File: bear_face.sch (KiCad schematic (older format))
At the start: 190 parts, among them J1 USB_B_Micro, SW1 SW_Push, U1 ATmega32U4-AU, Y1 16MHz

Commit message: Footprints updated
Changed footprints to copies saved in 'bear_face_parts' for ease of cloning
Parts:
- D1, D10, D11, D12, D13, D14, D15, D16, D17, D18, D19, D2, D20, D21, D22, D23, D24, D25, D26, D27, D28, D29, D3, D30, D31, D32, D33, D34, D35, D36, D37, D38, D39, D4, D40, D41, D42, D43, D44, D45, D46, D47, D48, D49, D5, D50, D51, D52, D53, D54, D55, D56, D57, D58, D59, D6, D60, D61, D62, D63, D64, D65, D66, D67, D68, D69, D7, D70, D71, D72, D73, D74, D75, D76, D77, D78, D79, D8, D80, D81, D82, D83, D9: footprint Keebio-Parts:Diode -> bear_face_parts:Diode-THT
- MX1, MX15, MX31, MX44: footprint MX_Only:MXOnly-1.5U-NoLED -> bear_face_parts:MXOnly-1.5U-NoLED
- MX10, MX11, MX12, MX13, MX14, MX16, MX17, MX18, MX19, MX2, MX20, MX21, MX22, MX23, MX24, MX25, MX26, MX27, MX28, MX3, MX30, MX32, MX33, MX34, MX35, MX36, MX37, MX38, MX39, MX4, MX40, MX41, MX42, MX43, MX45, MX47, MX48, MX49, MX5, MX50, MX51, MX52, MX53, MX54, MX55, MX56, MX57, MX59, MX6, MX61, MX62, MX63, MX64, MX65, MX66, MX67, MX68, MX69, MX7, MX70, MX72, MX73, MX78, MX79, MX8, MX80, MX81, MX82, MX83, MX9: footprint MX_Only:MXOnly-1U-NoLED -> bear_face_parts:MXOnly-1U-NoLED
- MX29: footprint MX_Only:MXOnly-2U-NoLED -> bear_face_parts:MXOnly-2U-NoLED
- MX46, MX71: footprint MX_Only:MXOnly-1.75U-NoLED -> bear_face_parts:MXOnly-1.75U-NoLED
- MX58, MX60: footprint MX_Only:MXOnly-2.25U-NoLED -> bear_face_parts:MXOnly-2.25U-NoLED
- MX74, MX75, MX76: footprint MX_Only:MXOnly-1.25U-NoLED -> bear_face_parts:MXOnly-1.25U-NoLED
- MX77: footprint MX_Only:MXOnly-6.25U-ReversedStabilizers-NoLED -> bear_face_parts:MXOnly-6.25U-ReversedStabilizers-NoLED
- SW1: footprint random-keyboard-parts:PushButton_6x6mm_TH_Pretty -> bear_face_parts:PushButton_6x6mm_TH_Pretty

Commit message: Initial SMD commit
Diodes changed to SMD, short tracks added to pad2 and between adjacent diodes
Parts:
- D1, D10, D11, D12, D13, D14, D15, D16, D17, D18, D19, D2, D20, D21, D22, D23, D24, D25, D26, D27, D28, D29, D3, D30, D31, D32, D33, D34, D35, D36, D37, D38, D39, D4, D40, D41, D42, D43, D44, D45, D46, D47, D48, D49, D5, D50, D51, D52, D53, D54, D55, D56, D57, D58, D59, D6, D60, D61, D62, D63, D64, D65, D66, D67, D68, D69, D7, D70, D71, D72, D73, D74, D75, D76, D77, D78, D79, D8, D80, D81, D82, D83, D9: footprint bear_face_parts:Diode-THT -> bear_face_parts:D_SOD-123

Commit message: Changed RESET switch to SMD
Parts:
- SW1: footprint bear_face_parts:PushButton_6x6mm_TH_Pretty -> random-keyboard-parts:SKQG-1155865
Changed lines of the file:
@@
 F 0 "SW1" H 1400 4085 50  0000 C CNN
 F 1 "SW_Push" H 1400 3994 50  0000 C CNN
-F 2 "bear_face_parts:PushButton_6x6mm_TH_Pretty" H 1400 4000 50  0001 C CNN
+F 2 "random-keyboard-parts:SKQG-1155865" H 1400 4000 50  0001 C CNN
 F 3 "~" H 1400 4000 50  0001 C CNN
 	1    1400 3800

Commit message: dPairs, left side MCU tracked
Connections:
- net RD-: now reaches R3.1, U1.3 (D-)
- net RD+: now reaches R2.1, U1.4 (D+)
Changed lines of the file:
@@
 L power:+5V #PWR0110
 U 1 1 5E4994F7
-P 1350 4600
-F 0 "#PWR0110" H 1350 4450 50  0001 C CNN
-F 1 "+5V" H 1365 4773 50  0000 C CNN
-F 2 "" H 1350 4600 50  0001 C CNN
-F 3 "" H 1350 4600 50  0001 C CNN
-	1    1350 4600
+P 1700 4600
+F 0 "#PWR0110" H 1700 4450 50  0001 C CNN
+F 1 "+5V" H 1715 4773 50  0000 C CNN
+F 2 "" H 1700 4600 50  0001 C CNN
+F 3 "" H 1700 4600 50  0001 C CNN
+	1    1700 4600
 	1    0    0    -1
 $EndComp
@@
 Wire Wire Line
 	750  4450 1100 4450
-Wire Wire Line
-	1350 4600 1800 4600
-Wire Wire Line
-	1300 4800 1800 4800
-Wire Wire Line
-	1000 4900 1800 4900
 $Comp
 L Connector:USB_B_Micro J1
@@
 Text GLabel 3000 6700 2    50   Input ~ 0
 ROW5
-Text GLabel 3000 6400 2    50   Input ~ 0
-COL0
-Text GLabel 3000 6600 2    50   Input ~ 0
-COL1
-Text GLabel 3000 6500 2    50   Input ~ 0
-COL2
 Text GLabel 3000 6200 2    50   Input ~ 0
 COL3
@@
 NoConn ~ 3000 4700
 NoConn ~ 3000 4800
+Text GLabel 1350 4800 1    50   Input ~ 0
+RD+
+Text GLabel 1050 4900 3    50   Input ~ 0
+RD-
+Wire Wire Line
+	1700 4600 1800 4600
+Connection ~ 1050 4900
+Connection ~ 1350 4800
+Wire Wire Line
+	1050 4900 1800 4900
+Wire Wire Line
+	1000 4900 1050 4900
+Wire Wire Line
+	1350 4800 1800 4800
+Wire Wire Line
+	1300 4800 1350 4800
+Text GLabel 3000 6500 2    50   Input ~ 0
+COL2
+Text GLabel 3000 6600 2    50   Input ~ 0
+COL1
+Text GLabel 3000 6400 2    50   Input ~ 0
+COL0
 $EndSCHEMATC

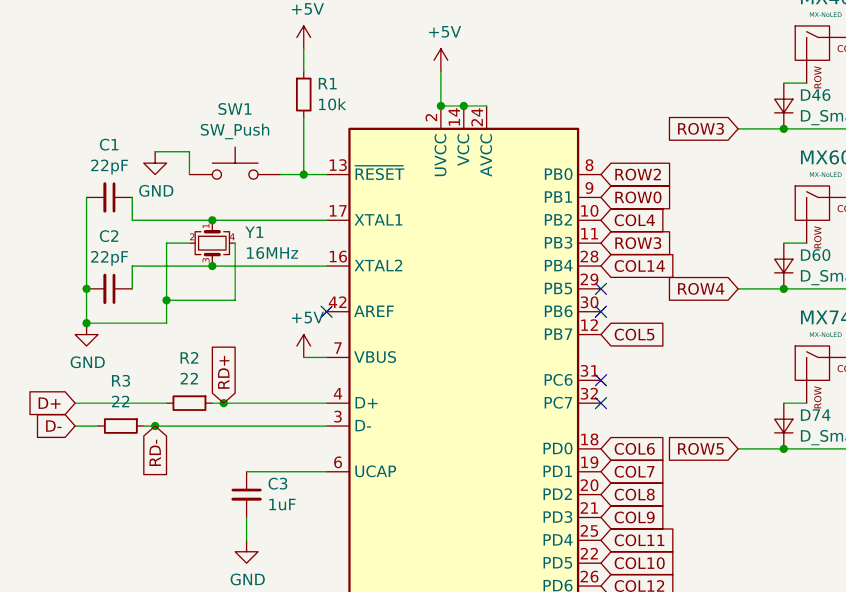
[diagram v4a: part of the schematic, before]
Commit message: Tracks finished, DRC check passed, tracks and vias cleaned up
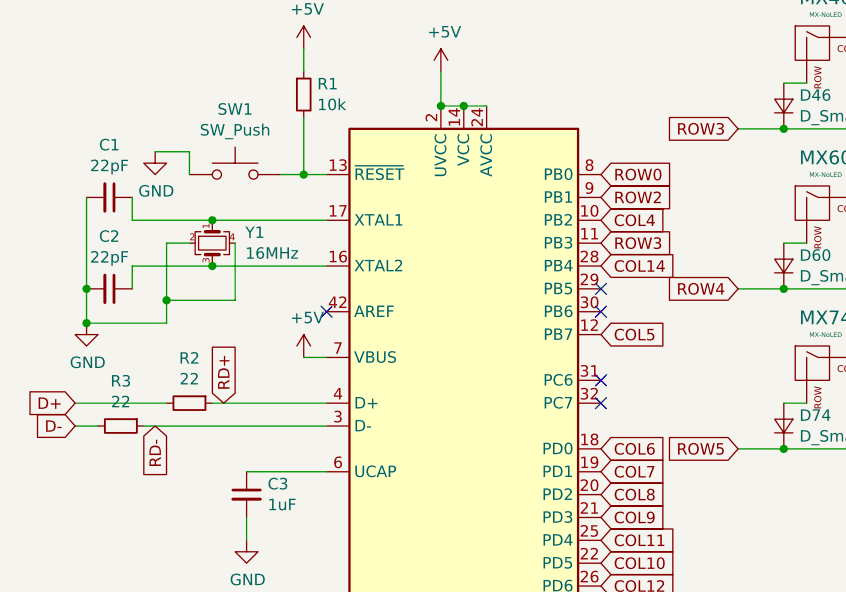
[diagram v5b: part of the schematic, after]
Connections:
- net ROW0: now also U1.8 (PB0); no longer U1.9 (PB1)
- net ROW2: now also U1.9 (PB1); no longer U1.8 (PB0)
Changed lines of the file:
@@
 COL3
 NoConn ~ 1800 4400
-Text GLabel 3000 3900 2    50   Input ~ 0
+Text GLabel 3000 3800 2    50   Input ~ 0
 ROW0
 Text GLabel 3000 6000 2    50   Input ~ 0
 ROW1
-Text GLabel 3000 3800 2    50   Input ~ 0
+Text GLabel 3000 3900 2    50   Input ~ 0
 ROW2
 Text GLabel 3000 4100 2    50   Input ~ 0
@@
 Text GLabel 3000 6300 2    50   Input ~ 0
 ROW4
-NoConn ~ 3000 4300
-NoConn ~ 3000 4400
-NoConn ~ 3000 4700
-NoConn ~ 3000 4800
 Text GLabel 1350 4800 1    50   Input ~ 0
 RD+
@@
 Wire Wire Line
 	1700 4600 1800 4600
-Connection ~ 1050 4900
-Connection ~ 1350 4800
-Wire Wire Line
-	1050 4900 1800 4900
-Wire Wire Line
-	1000 4900 1050 4900
-Wire Wire Line
-	1350 4800 1800 4800
-Wire Wire Line
-	1300 4800 1350 4800
 Text GLabel 3000 6500 2    50   Input ~ 0
 COL2
@@
 Text GLabel 3000 6400 2    50   Input ~ 0
 COL0
+Wire Wire Line
+	1000 4900 1800 4900
+Wire Wire Line
+	1300 4800 1800 4800
+NoConn ~ 3000 4300
+NoConn ~ 3000 4400
+NoConn ~ 3000 4700
+NoConn ~ 3000 4800
 $EndSCHEMATC

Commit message: Load caps moved closer, minor MCU track tweaks, USB-Micro changed to molex
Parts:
- J1: footprint Connector_USB:USB_Micro-B_Wuerth_629105150521 -> Connector_USB:USB_Micro-B_GCT_USB3076-30-A
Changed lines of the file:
@@
 F 0 "J1" H 1257 2867 50  0000 C CNN
 F 1 "USB_B_Micro" H 1257 2776 50  0000 C CNN
-F 2 "Connector_USB:USB_Micro-B_Wuerth_629105150521" H 1350 2350 50  0001 C CNN
+F 2 "Connector_USB:USB_Micro-B_GCT_USB3076-30-A" H 1350 2350 50  0001 C CNN
 F 3 "~" H 1350 2350 50  0001 C CNN
 	1    1200 2400

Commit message: Initial branch commit
Footprint SilkS updated to be on desired sides, all components placed
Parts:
- added Q1: 2N7002, Package_TO_SOT_SMD:SOT-23, symbol Transistor_FET:2N7002
- added R1, R10, R11, R12, R13, R14, R15, R16, R17, R18, R19, R2, R20, R21, R22, R23, R24, R25, R26, R27, R28, R29, R3, R30, R31, R32, R33, R34, R35, R36, R37, R38, R39, R4, R40, R41, R42, R43, R44, R45, R46, R47, R48, R49, R5, R50, R51, R52, R53, R54, R55, R56, R57, R58, R59, R6, R60, R61, R62, R63, R64, R65, R66, R67, R68, R69, R7, R70, R71, R72, R73, R74, R75, R76, R77, R78, R79, R8, R80, R81, R82, R83, R9: 470, bear_face_parts:Resistor-THT, symbol Device:R_Small
- added R88: 4.7k, Keebio-Parts:Resistor, symbol Device:R_Small
- D1, D10, D11, D12, D13, D14, D15, D16, D17, D18, D19, D2, D20, D21, D22, D23, D24, D25, D26, D27, D28, D29, D3, D30, D31, D32, D33, D34, D35, D36, D37, D38, D39, D4, D40, D41, D42, D43, D44, D45, D46, D47, D48, D49, D5, D50, D51, D52, D53, D54, D55, D56, D57, D58, D59, D6, D60, D61, D62, D63, D64, D65, D66, D67, D68, D69, D7, D70, D71, D72, D73, D74, D75, D76, D77, D78, D79, D8, D80, D81, D82, D83, D9: footprint bear_face_parts:D_SOD-123 -> bear_face_parts:Diode-THT
- H1, H2, H3, H4, H5, H6, H7: footprint MountingHole:MountingHole_6mm -> bear_face_parts:MountingHole_6mm
- H8: footprint MountingHole:MountingHole_3mm -> bear_face_parts:MountingHole_3mm
- J1: footprint Connector_USB:USB_Micro-B_GCT_USB3076-30-A -> Connector_USB:USB_Micro-B_Wuerth_629105150521
- MX1, MX15, MX31, MX44: value MX-NoLED -> MX-LED; footprint bear_face_parts:MXOnly-1.5U-NoLED -> bear_face_parts:MXOnly-1.5U; symbol MX_Alps_Hybrid:MX-NoLED -> MX_Alps_Hybrid:MX-LED
- MX10, MX11, MX12, MX13, MX14, MX16, MX17, MX18, MX19, MX2, MX20, MX21, MX22, MX23, MX24, MX25, MX26, MX27, MX28, MX3, MX30, MX32, MX33, MX34, MX35, MX36, MX37, MX38, MX39, MX4, MX40, MX41, MX42, MX43, MX45, MX47, MX48, MX49, MX5, MX50, MX51, MX52, MX53, MX54, MX55, MX56, MX57, MX59, MX6, MX61, MX62, MX63, MX64, MX65, MX66, MX67, MX68, MX69, MX7, MX70, MX72, MX73, MX78, MX79, MX8, MX80, MX81, MX82, MX83, MX9: value MX-NoLED -> MX-LED; footprint bear_face_parts:MXOnly-1U-NoLED -> bear_face_parts:MXOnly-1U; symbol MX_Alps_Hybrid:MX-NoLED -> MX_Alps_Hybrid:MX-LED
- MX29: value MX-NoLED -> MX-LED; footprint bear_face_parts:MXOnly-2U-NoLED -> bear_face_parts:MXOnly-2U-NoStabs; symbol MX_Alps_Hybrid:MX-NoLED -> MX_Alps_Hybrid:MX-LED
- MX46, MX71: value MX-NoLED -> MX-LED; footprint bear_face_parts:MXOnly-1.75U-NoLED -> bear_face_parts:MXOnly-1.75U; symbol MX_Alps_Hybrid:MX-NoLED -> MX_Alps_Hybrid:MX-LED
- MX58, MX60: value MX-NoLED -> MX-LED; footprint bear_face_parts:MXOnly-2.25U-NoLED -> bear_face_parts:MXOnly-2.25U-NoStabs; symbol MX_Alps_Hybrid:MX-NoLED -> MX_Alps_Hybrid:MX-LED
- MX74, MX75, MX76: value MX-NoLED -> MX-LED; footprint bear_face_parts:MXOnly-1.25U-NoLED -> bear_face_parts:MXOnly-1.25U; symbol MX_Alps_Hybrid:MX-NoLED -> MX_Alps_Hybrid:MX-LED
- MX77: value MX-NoLED -> MX-LED; footprint bear_face_parts:MXOnly-6.25U-ReversedStabilizers-NoLED -> bear_face_parts:MXOnly-6.25U-NoStabs; symbol MX_Alps_Hybrid:MX-NoLED -> MX_Alps_Hybrid:MX-LED
- SW1: footprint random-keyboard-parts:SKQG-1155865 -> bear_face_parts:PushButton_6x6mm_TH_Pretty
- renumbered R1 to R84, R2 to R85, R3 to R86, R4 to R87
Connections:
- net +5V: now also MX1.3 (LED), MX10.3 (LED), MX11.3 (LED), MX12.3 (LED), MX13.3 (LED), MX14.3 (LED), MX15.3 (LED), MX16.3 (LED), MX17.3 (LED), MX18.3 (LED), MX19.3 (LED), MX2.3 (LED), MX20.3 (LED), MX21.3 (LED), MX22.3 (LED), MX23.3 (LED), MX24.3 (LED), MX25.3 (LED), MX26.3 (LED), MX27.3 (LED), MX28.3 (LED), MX29.3 (LED), MX3.3 (LED), MX30.3 (LED), MX31.3 (LED), MX32.3 (LED), MX33.3 (LED), MX34.3 (LED), MX35.3 (LED), MX36.3 (LED), MX37.3 (LED), MX38.3 (LED), MX39.3 (LED), MX4.3 (LED), MX40.3 (LED), MX41.3 (LED), MX42.3 (LED), MX43.3 (LED), MX44.3 (LED), MX45.3 (LED), MX46.3 (LED), MX47.3 (LED), MX48.3 (LED), MX49.3 (LED), MX5.3 (LED), MX50.3 (LED), MX51.3 (LED), MX52.3 (LED), MX53.3 (LED), MX54.3 (LED), MX55.3 (LED), MX56.3 (LED), MX57.3 (LED), MX58.3 (LED), MX59.3 (LED), MX6.3 (LED), MX60.3 (LED), MX61.3 (LED), MX62.3 (LED), MX63.3 (LED), MX64.3 (LED), MX65.3 (LED), MX66.3 (LED), MX67.3 (LED), MX68.3 (LED), MX69.3 (LED), MX7.3 (LED), MX70.3 (LED), MX71.3 (LED), MX72.3 (LED), MX73.3 (LED), MX74.3 (LED), MX75.3 (LED), MX76.3 (LED), MX77.3 (LED), MX78.3 (LED), MX79.3 (LED), MX8.3 (LED), MX80.3 (LED), MX81.3 (LED), MX82.3 (LED), MX83.3 (LED), MX9.3 (LED)
- net GND: now also Q1.2 (S), R88.2
- net LEDPIN: now reaches U1.29 (PB5)
- net LEDPIN: now also Q1.1 (G), R88.1
- new net: MX46.4 (LEDGND), R46.1
- new net: MX60.4 (LEDGND), R60.1
- new net: MX74.4 (LEDGND), R74.1
- new net: MX75.4 (LEDGND), R75.1
- new net: MX76.4 (LEDGND), R76.1
- new net: MX3.4 (LEDGND), R3.1
- new net: MX18.4 (LEDGND), R18.1
- new net: MX17.4 (LEDGND), R17.1
- new net: MX32.4 (LEDGND), R32.1
- new net: MX33.4 (LEDGND), R33.1
- new net: MX48.4 (LEDGND), R48.1
- new net: MX47.4 (LEDGND), R47.1
- new net: MX61.4 (LEDGND), R61.1
- new net: MX62.4 (LEDGND), R62.1
- new net: MX5.4 (LEDGND), R5.1
- new net: MX4.4 (LEDGND), R4.1
- new net: MX19.4 (LEDGND), R19.1
- new net: MX34.4 (LEDGND), R34.1
- new net: MX35.4 (LEDGND), R35.1
- new net: MX50.4 (LEDGND), R50.1
- new net: MX49.4 (LEDGND), R49.1
- new net: MX63.4 (LEDGND), R63.1
- new net: MX64.4 (LEDGND), R64.1
- new net: MX6.4 (LEDGND), R6.1
- new net: MX20.4 (LEDGND), R20.1
- new net: MX21.4 (LEDGND), R21.1
- new net: MX22.4 (LEDGND), R22.1
- new net: MX37.4 (LEDGND), R37.1
- new net: MX36.4 (LEDGND), R36.1
- new net: MX51.4 (LEDGND), R51.1
- new net: MX65.4 (LEDGND), R65.1
- new net: MX77.4 (LEDGND), R77.1
- new net: MX7.4 (LEDGND), R7.1
- new net: MX8.4 (LEDGND), R8.1
- new net: MX24.4 (LEDGND), R24.1
- new net: MX23.4 (LEDGND), R23.1
- new net: MX38.4 (LEDGND), R38.1
- new net: MX39.4 (LEDGND), R39.1
- new net: MX53.4 (LEDGND), R53.1
- new net: MX52.4 (LEDGND), R52.1
- new net: MX66.4 (LEDGND), R66.1
- new net: MX9.4 (LEDGND), R9.1
- new net: MX10.4 (LEDGND), R10.1
- new net: MX26.4 (LEDGND), R26.1
- new net: MX25.4 (LEDGND), R25.1
- new net: MX40.4 (LEDGND), R40.1
- new net: MX41.4 (LEDGND), R41.1
- new net: MX55.4 (LEDGND), R55.1
- new net: MX54.4 (LEDGND), R54.1
- new net: MX67.4 (LEDGND), R67.1
- new net: MX2.4 (LEDGND), R2.1
- new net: MX1.4 (LEDGND), R1.1
- new net: MX16.4 (LEDGND), R16.1
- new net: MX12.4 (LEDGND), R12.1
- new net: MX11.4 (LEDGND), R11.1
- new net: MX27.4 (LEDGND), R27.1
- new net: MX28.4 (LEDGND), R28.1
- new net: MX42.4 (LEDGND), R42.1
- new net: MX57.4 (LEDGND), R57.1
- new net: MX56.4 (LEDGND), R56.1
- new net: MX69.4 (LEDGND), R69.1
- new net: MX68.4 (LEDGND), R68.1
- new net: MX31.4 (LEDGND), R31.1
- new net: MX13.4 (LEDGND), R13.1
- new net: MX14.4 (LEDGND), R14.1
- new net: MX29.4 (LEDGND), R29.1
- new net: MX44.4 (LEDGND), R44.1
- new net: MX43.4 (LEDGND), R43.1
- new net: MX58.4 (LEDGND), R58.1
- new net: MX71.4 (LEDGND), R71.1
- new net: MX70.4 (LEDGND), R70.1
- new net: MX78.4 (LEDGND), R78.1
- new net: MX45.4 (LEDGND), R45.1
- new net: MX59.4 (LEDGND), R59.1
- new net: MX72.4 (LEDGND), R72.1
- new net: MX73.4 (LEDGND), R73.1
- new net: MX83.4 (LEDGND), R83.1
- new net: MX82.4 (LEDGND), R82.1
- new net: MX81.4 (LEDGND), R81.1
- new net: MX80.4 (LEDGND), R80.1
- new net: MX79.4 (LEDGND), R79.1
- new net: MX15.4 (LEDGND), R15.1
- new net: MX30.4 (LEDGND), R30.1
- new net LEDOUT: Q1.3 (D), R1.2, R10.2, R11.2, R12.2, R13.2, R14.2, R15.2, R16.2, R17.2, R18.2, R19.2, R2.2, R20.2, R21.2, R22.2, R23.2, R24.2, R25.2, R26.2, R27.2, R28.2, R29.2, R3.2, R30.2, R31.2, R32.2, R33.2, R34.2, R35.2, R36.2, R37.2, R38.2, R39.2, R4.2, R40.2, R41.2, R42.2, R43.2, R44.2, R45.2, R46.2, R47.2, R48.2, R49.2, R5.2, R50.2, R51.2, R52.2, R53.2, R54.2, R55.2, R56.2, R57.2, R58.2, R59.2, R6.2, R60.2, R61.2, R62.2, R63.2, R64.2, R65.2, R66.2, R67.2, R68.2, R69.2, R7.2, R70.2, R71.2, R72.2, R73.2, R74.2, R75.2, R76.2, R77.2, R78.2, R79.2, R8.2, R80.2, R81.2, R82.2, R83.2, R9.2
- no-connect marks 5 -> 6
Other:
- moved on the sheet: D1, D10, D11, D12, D13, D14, D15, D16, D17, D18, D19, D2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

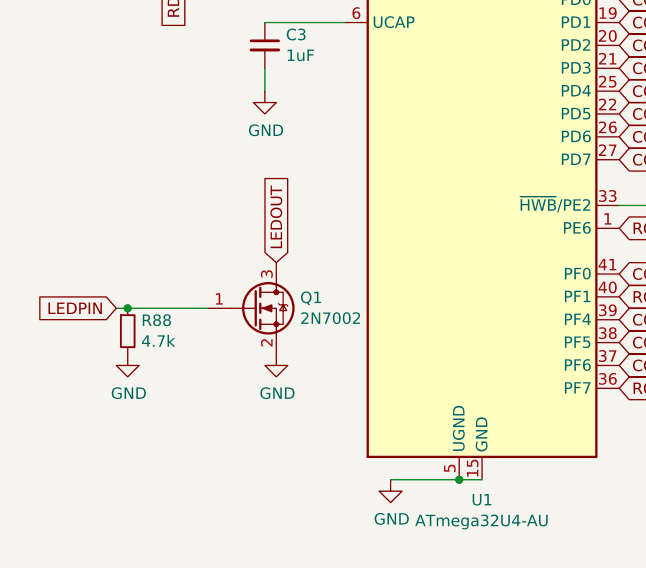
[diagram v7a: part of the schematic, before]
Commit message: Minor sch tweaks for MOSFET
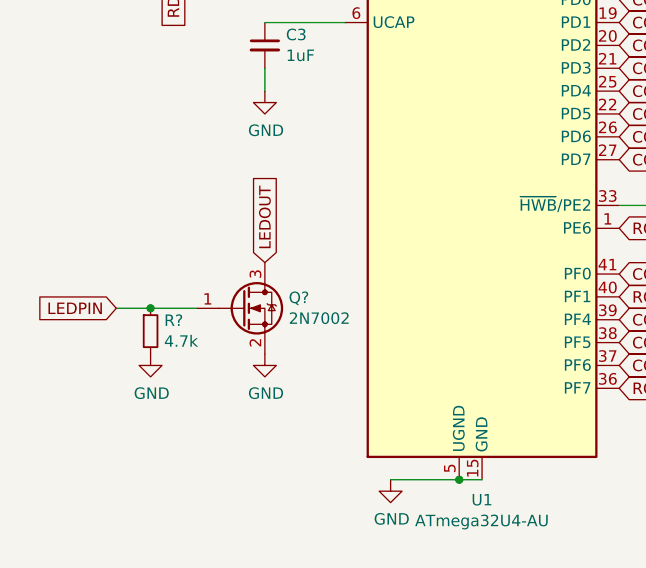
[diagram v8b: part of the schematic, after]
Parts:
- removed Q1: 2N7002, Package_TO_SOT_SMD:SOT-23, symbol Transistor_FET:2N7002
- removed R88: 4.7k, Keebio-Parts:Resistor, symbol Device:R_Small
- added Q?: 2N7002, Package_TO_SOT_SMD:SOT-23, symbol Transistor_FET:2N7002
- added R?: 4.7k, symbol Device:R_Small
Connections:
- net GND: now also Q?.2 (S), R?.2
- net LEDOUT: now also Q?.3 (D)
- net LEDPIN: now also Q?.1 (G), R?.1
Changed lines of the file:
@@
 Text GLabel 3000 4300 2    50   Input ~ 0
 LEDPIN
-$Comp
-L Transistor_FET:2N7002 Q1
-U 1 1 5E2B0FD7
-P 1400 6350
-F 0 "Q1" H 1604 6396 50  0000 L CNN
-F 1 "2N7002" H 1604 6305 50  0000 L CNN
-F 2 "Package_TO_SOT_SMD:SOT-23" H 1600 6275 50  0001 L CIN
-F 3 "https://www.fairchildsemi.com/datasheets/2N/2N7002.pdf" H 1400 6350 50  0001 L CNN
-	1    1400 6350
-	1    0    0    -1
-$EndComp
-Text GLabel 800  6350 0    50   Input ~ 0
-LEDPIN
-$Comp
-L Device:R_Small R88
-U 1 1 5E2D6A00
-P 850 6450
-F 0 "R88" H 909 6496 50  0000 L CNN
-F 1 "4.7k" H 909 6405 50  0000 L CNN
-F 2 "Keebio-Parts:Resistor" H 850 6450 50  0001 C CNN
-F 3 "~" H 850 6450 50  0001 C CNN
-	1    850  6450
-	1    0    0    -1
-$EndComp
-Wire Wire Line
-	850  6350 1200 6350
-$Comp
-L power:GND #PWR012
-U 1 1 5E2D8122
-P 850 6550
-F 0 "#PWR012" H 850 6300 50  0001 C CNN
-F 1 "GND" H 855 6377 50  0000 C CNN
-F 2 "" H 850 6550 50  0001 C CNN
-F 3 "" H 850 6550 50  0001 C CNN
-	1    850  6550
-	1    0    0    -1
-$EndComp
-$Comp
-L power:GND #PWR013
-U 1 1 5E2D97E0
-P 1500 6550
-F 0 "#PWR013" H 1500 6300 50  0001 C CNN
-F 1 "GND" H 1505 6377 50  0000 C CNN
-F 2 "" H 1500 6550 50  0001 C CNN
-F 3 "" H 1500 6550 50  0001 C CNN
-	1    1500 6550
-	1    0    0    -1
-$EndComp
-Text GLabel 1500 6150 1    50   Input ~ 0
-LEDOUT
 Text GLabel 3350 1100 1    50   Input ~ 0
 LEDOUT
@@
 Wire Wire Line
 	3450 1100 3450 1800
-Wire Wire Line
-	800  6350 850  6350
-Connection ~ 850  6350
 Connection ~ 3850 3850
 Connection ~ 3850 3150
@@
 Wire Wire Line
 	1200 4300 1200 4400
+Text GLabel 800  6350 0    50   Input ~ 0
+LEDPIN
+$Comp
+L Transistor_FET:2N7002 Q?
+U 1 1 5E2E1EE1
+P 1350 6350
+F 0 "Q?" H 1554 6396 50  0000 L CNN
+F 1 "2N7002" H 1554 6305 50  0000 L CNN
+F 2 "Package_TO_SOT_SMD:SOT-23" H 1550 6275 50  0001 L CIN
+F 3 "https://www.fairchildsemi.com/datasheets/2N/2N7002.pdf" H 1350 6350 50  0001 L CNN
+	1    1350 6350
+	1    0    0    -1
+$EndComp
+Text GLabel 1450 6150 1    50   Input ~ 0
+LEDOUT
+$Comp
+L power:GND #PWR?
+U 1 1 5E2E9481
+P 1450 6550
+F 0 "#PWR?" H 1450 6300 50  0001 C CNN
+F 1 "GND" H 1455 6377 50  0000 C CNN
+F 2 "" H 1450 6550 50  0001 C CNN
+F 3 "" H 1450 6550 50  0001 C CNN
+	1    1450 6550
+	1    0    0    -1
+$EndComp
+Wire Wire Line
+	800  6350 950  6350
+$Comp
+L Device:R_Small R?
+U 1 1 5E33D046
+P 950 6450
+F 0 "R?" H 1009 6496 50  0000 L CNN
+F 1 "4.7k" H 1009 6405 50  0000 L CNN
+F 2 "" H 950 6450 50  0001 C CNN
+F 3 "~" H 950 6450 50  0001 C CNN
+	1    950  6450
+	1    0    0    -1
+$EndComp
+Connection ~ 950  6350
+Wire Wire Line
+	950  6350 1150 6350
+$Comp
+L power:GND #PWR?
+U 1 1 5E33ECD1
+P 950 6550
+F 0 "#PWR?" H 950 6300 50  0001 C CNN
+F 1 "GND" H 955 6377 50  0000 C CNN
+F 2 "" H 950 6550 50  0001 C CNN
+F 3 "" H 950 6550 50  0001 C CNN
+	1    950  6550
+	1    0    0    -1
+$EndComp
 $EndSCHEMATC
